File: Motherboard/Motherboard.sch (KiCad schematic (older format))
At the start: 2 parts

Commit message: Labeled RPi GPIO pin and MCP3008. Need 5v external
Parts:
- added J?: Power In, symbol Connector_Generic:Conn_01x04
- added J?: Moisture 0, symbol Connector_Generic:Conn_01x03
- added R? (x2): R, Resistor_SMD:R_0603_1608Metric_Pad1.05x0.95mm_HandSolder, symbol Device:R
- added U?: BME280, Package_LGA:Bosch_LGA-8_2.5x2.5mm_P0.65mm_ClockwisePinNumbering, symbol Sensor:BME280
- J?: value Conn_02x20_Odd_Even -> RPi 3B+
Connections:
- net labels added: +5VA, A0, GPIO_0, GPIO_1, GPIO_10-MOSI, GPIO_11-SCLK, GPIO_12-PWM0, GPIO_13-PWM1, GPIO_14-TX, GPIO_15-RX, GPIO_16, GPIO_17, GPIO_18-CLK, GPIO_19-PCMFS, GPIO_2-SDA, GPIO_20, GPIO_21, GPIO_22, GPIO_23, GPIO_24, GPIO_25, GPIO_26, GPIO_27, GPIO_3-SCL, GPIO_4-GPCLK0, GPIO_5, GPIO_6, GPIO_7-CE1, GPIO_8-CE0, GPIO_9-MISO
- net labels removed: GPIO2-SDA, GPIO3-SCL
- wire segments 7 -> 72
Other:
- moved on the sheet: J?, U?

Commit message: BME280
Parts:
- added C? (x2): 0.1 uF, Capacitor_SMD:C_0603_1608Metric_Pad1.05x0.95mm_HandSolder, symbol Device:C
- added D? (x2): LED, LED_SMD:LED_0603_1608Metric_Pad1.05x0.95mm_HandSolder, symbol Device:LED
- added R? (x2): 4.7 kohm, Resistor_SMD:R_0603_1608Metric_Pad1.05x0.95mm_HandSolder, symbol Device:R
- added R? (x2): R, Resistor_SMD:R_0603_1608Metric_Pad1.05x0.95mm_HandSolder, symbol Device:R
- U?: Digi-Key # (none) -> 828-1063-1-ND; Digi-Key Link (none) -> https://www.digikey.ca/en/products/detail/bosch-sensortec/B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; Manufacturer (none) -> Bosch Sensortec; Manufacturer # (none) -> BME280
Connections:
- wire segments 72 -> 99
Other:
- moved on the sheet: U?

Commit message: Need to find an ambient light sensor
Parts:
- removed J?: Power In, symbol Connector_Generic:Conn_01x04
- added C?: 1 uF, Capacitor_SMD:C_0603_1608Metric_Pad1.05x0.95mm_HandSolder, symbol Device:C
- added J?: Barrel_Jack, symbol Connector:Barrel_Jack
- added J?: Moisture 1, symbol Connector_Generic:Conn_01x03
- added J?: Moisture 2, symbol Connector_Generic:Conn_01x03
- added J?: Moisture 3, symbol Connector_Generic:Conn_01x03
- added J?: Moisture 4, symbol Connector_Generic:Conn_01x03
- added J?: Moisture 5, symbol Connector_Generic:Conn_01x03
- added J?: AUX Analog A, symbol Connector_Generic:Conn_01x03
- added J?: AUX Analog B, symbol Connector_Generic:Conn_01x03
- added J?: AUX Digital A, symbol Connector_Generic:Conn_01x03
- added J?: AUX Digital B, symbol Connector_Generic:Conn_01x03
- added R? (x10): R, Resistor_SMD:R_0603_1608Metric_Pad1.05x0.95mm_HandSolder, symbol Device:R
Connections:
- net labels added: A1, A2, A3, A4, A5, A6, A7, D12, D13
- wire segments 99 -> 162
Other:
- note added: "0x76"
- note added: "Ambient Light"
- note added: "Analog to Digital Converter (ADC)"
- note added: "Auxilary"
- note added: "Power In"
- note added: "Pressure, Humidity, and Temperature"
- note added: "RPi Interface"
- note added: "Soil Moisture Sensors"
- moved on the sheet: C?, D?, J?, R?, U?

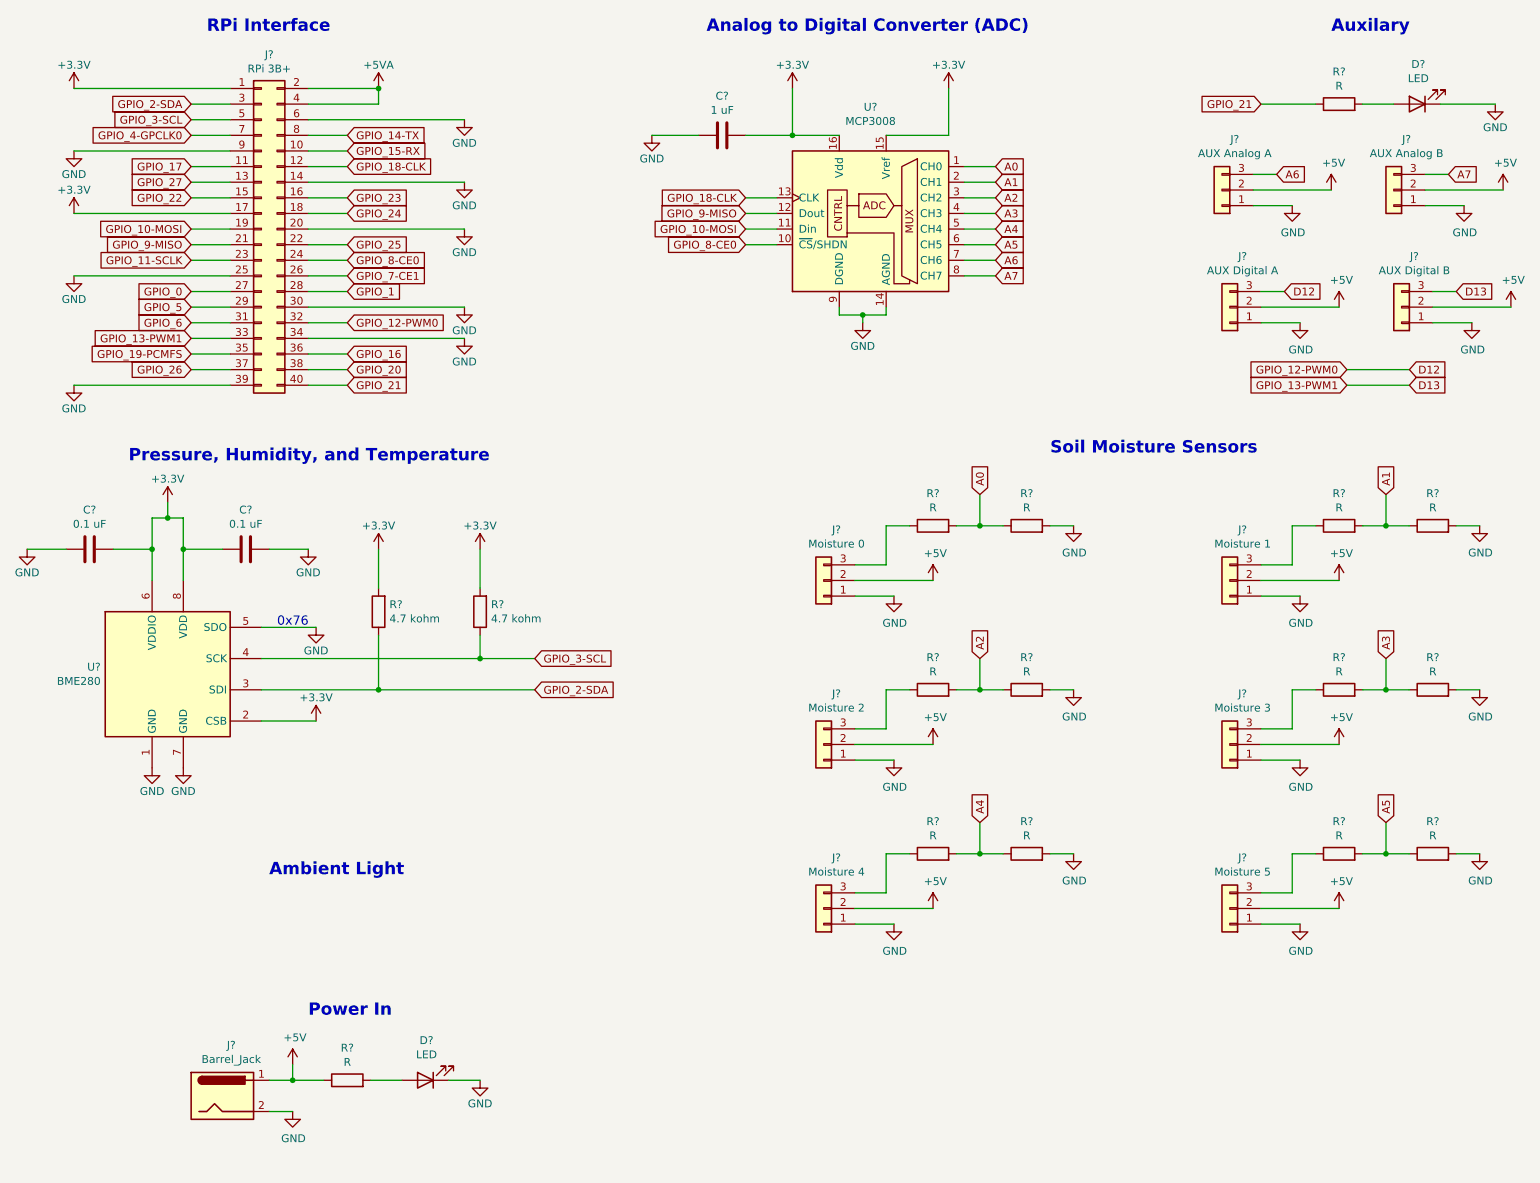
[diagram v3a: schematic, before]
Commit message: schematic looks mostly routed, need to finalize components
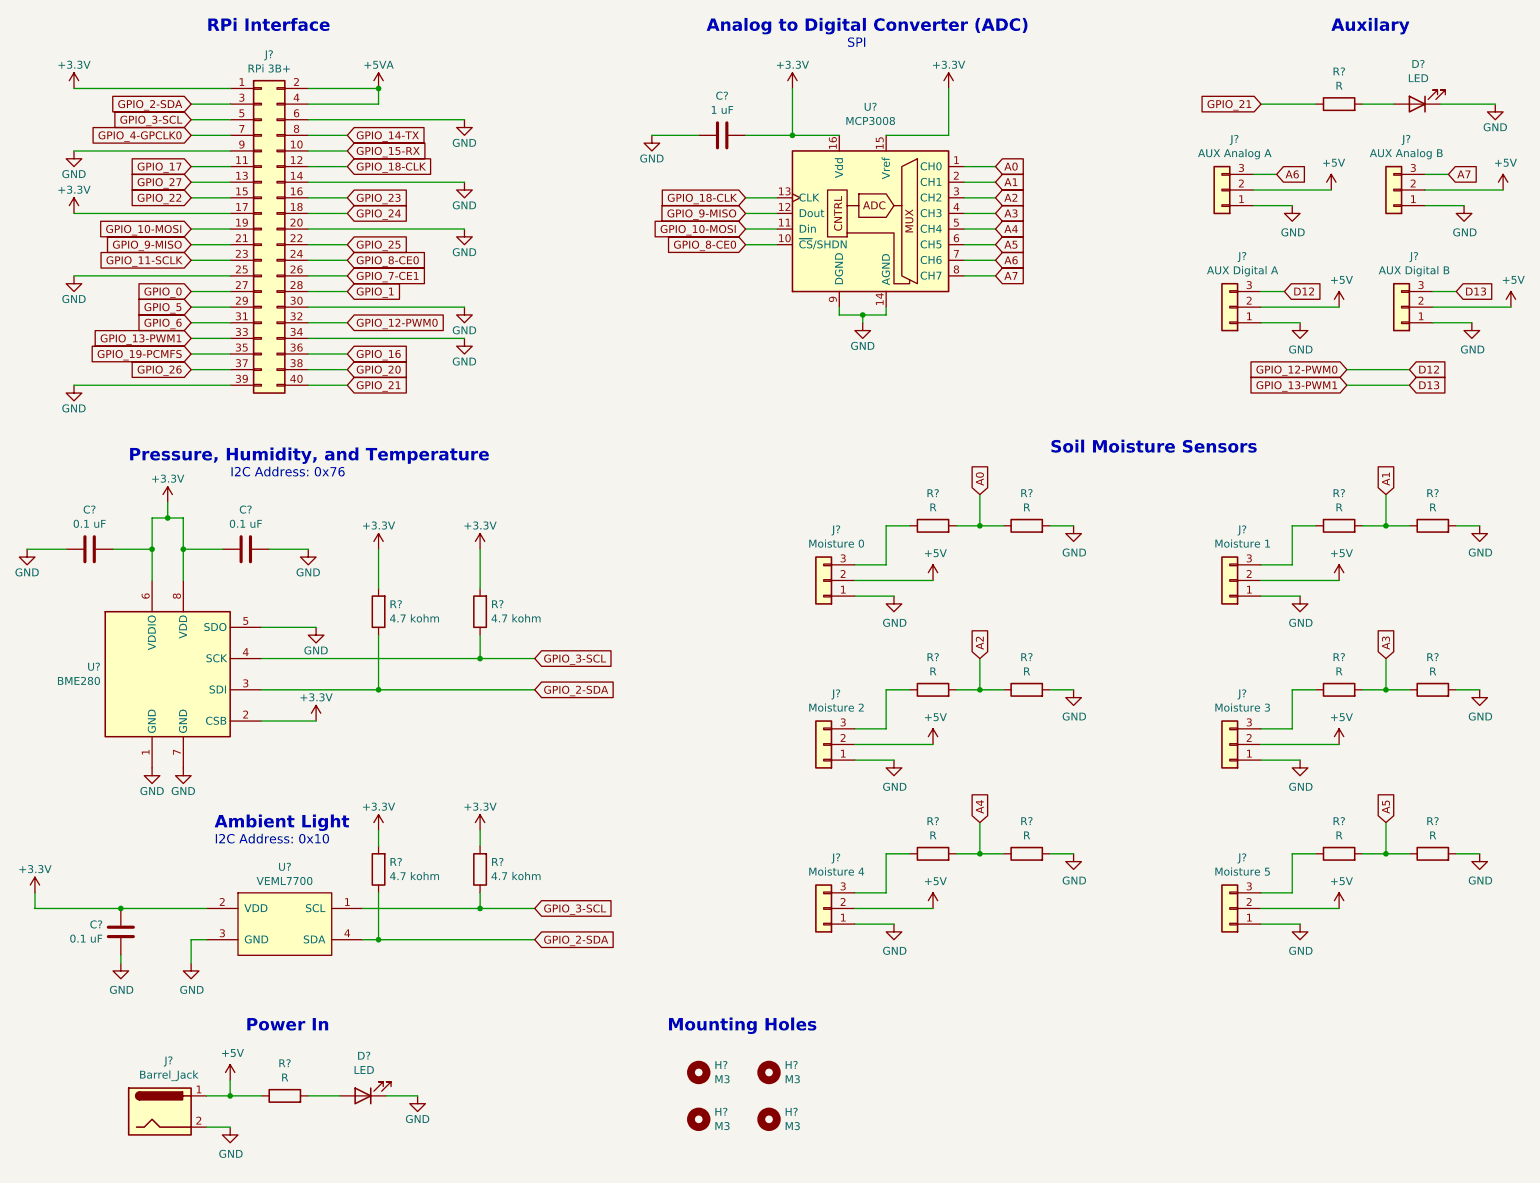
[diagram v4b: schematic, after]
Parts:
- added C?: 0.1 uF, Capacitor_SMD:C_0603_1608Metric_Pad1.05x0.95mm_HandSolder, symbol Device:C
- added H? (x4): M3, MountingHole:MountingHole_3.2mm_M3_ISO7380_Pad, symbol Mechanical:MountingHole
- added R? (x2): 4.7 kohm, Resistor_SMD:R_0603_1608Metric_Pad1.05x0.95mm_HandSolder, symbol Device:R
- added U?: VEML7700, symbol Custom:VEML7700
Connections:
- net +3V3: now also C?.1, R?.2, R?.2, U?.2 (VDD)
- net GND: now also C?.2, U?.3 (GND)
- net GPIO_2-SDA: now also R?.1, U?.4 (SDA)
- net GPIO_3-SCL: now also R?.1, U?.1 (SCL)
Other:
- note added: "I2C Address: 0x10"
- note added: "I2C Address: 0x76"
- note added: "Mounting Holes"
- note added: "SPI"
- note removed: "0x76"
- moved on the sheet: D?, J?, R?

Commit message: Schematic mostly done, just need to double check
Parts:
- removed J?: Barrel_Jack, symbol Connector:Barrel_Jack
- added J12: Power In, symbol Connector:Barrel_Jack_Switch
- J1, J10, J11, J2, J4, J5, J6, J7, J8, J9: renamed from J?; footprint (none) -> Connector_PinHeader_2.54mm:PinHeader_1x03_P2.54mm_Vertical
- J3: renamed from J?; footprint (none) -> Connector_PinHeader_2.54mm:PinHeader_2x20_P2.54mm_Vertical
- U3: renamed from U?; footprint (none) -> Custom:VEML7700
- gave numbers to parts that had none: 30
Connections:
- net +5V: now also J12.1
- net GND: now also J12.2, J12.3
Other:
- moved on the sheet: C1, D2, H1, H2, H3, H4, R18, U1

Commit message: Quick layout before schematic review
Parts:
- J12: footprint (none) -> Connector_BarrelJack:BarrelJack_CUI_PJ-102AH_Horizontal
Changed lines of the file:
@@
 F 0 "J12" H 1607 7867 50  0000 C CNN
 F 1 "Power In" H 1607 7776 50  0000 C CNN
-F 2 "" H 1600 7510 50  0001 C CNN
+F 2 "Connector_BarrelJack:BarrelJack_CUI_PJ-102AH_Horizontal" H 1600 7510 50  0001 C CNN
 F 3 "~" H 1600 7510 50  0001 C CNN
 	1    1550 7550

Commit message: Schematic is fully reviewed
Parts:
- removed R1: R, Resistor_SMD:R_0603_1608Metric_Pad1.05x0.95mm_HandSolder, symbol Device:R
- added C5: 1 uF, Capacitor_SMD:C_0603_1608Metric_Pad1.05x0.95mm_HandSolder, symbol Device:C
- D1: value LED -> Blue 3.3V 20mA
- D2: value LED -> Green 2.2V 20mA
- J12: Digi-Key # (none) -> CP-102AH-ND; Digi-Key Link (none) -> https://www.digikey.ca/en/products/detail/cui-devices/PJ-10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; Manufacturer (none) -> CUI Devices; Manufacturer # (none) -> PJ-102AH
- R10, R12, R14, R2, R4, R8: value R -> 1.7 kohm
- R11, R13, R15, R3, R5, R9: value R -> 3.3 kohm
- R18: value R -> 150 ohm
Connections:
- net +3V3: now also C5.1
- net GND: now also C5.2
- net GPIO_11-SCLK: now also U1.13 (CLK)
- net GPIO_18-CLK: no longer U1.13 (CLK)
- net GPIO_21: now also D1.2 (A)
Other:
- note added: "Voltage divider from 5V -> 3.3V"
- moved on the sheet: C2, C3, C4, D1, H1, H2, H3, H4, J12, J3, R16, R17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

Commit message: added missing footprint on new cap
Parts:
- C5: footprint Capacitor_SMD:C_0603_1608Metric_Pad1.05x0.95mm_HandSolder -> Capacitor_SMD:C_0603_1608Metric_Pad1.08x0.95mm_HandSolder
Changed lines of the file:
@@
 F 0 "C5" V 7302 1450 50  0000 C CNN
 F 1 "1 uF" V 7211 1450 50  0000 C CNN
-F 2 "Capacitor_SMD:C_0603_1608Metric_Pad1.05x0.95mm_HandSolder" H 7088 1300 50  0001 C CNN
+F 2 "Capacitor_SMD:C_0603_1608Metric_Pad1.08x0.95mm_HandSolder" H 7088 1300 50  0001 C CNN
 F 3 "~" H 7050 1450 50  0001 C CNN
 	1    7050 1450
